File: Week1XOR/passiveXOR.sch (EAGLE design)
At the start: 27 parts

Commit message: First routing Started
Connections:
- removed net COUT: R7.2
- new net OUTC: JP1.4, R7.2
- net A: no longer JP1.2
- net B: no longer JP1.3
- net C: no longer JP1.4
- net INA: now also JP1.2
- net INB: now also JP1.3

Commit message: More routing and schmatic fixes
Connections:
- removed net VCC: JP1.1, JP2.1
- net A: no longer JP2.2
- net B: no longer JP2.3
- net C: no longer JP2.4
- net INA: now also JP2.2
- net INB: now also JP2.3
- net OUTC: now also JP2.4
- net VDD: now also JP1.1, JP2.1

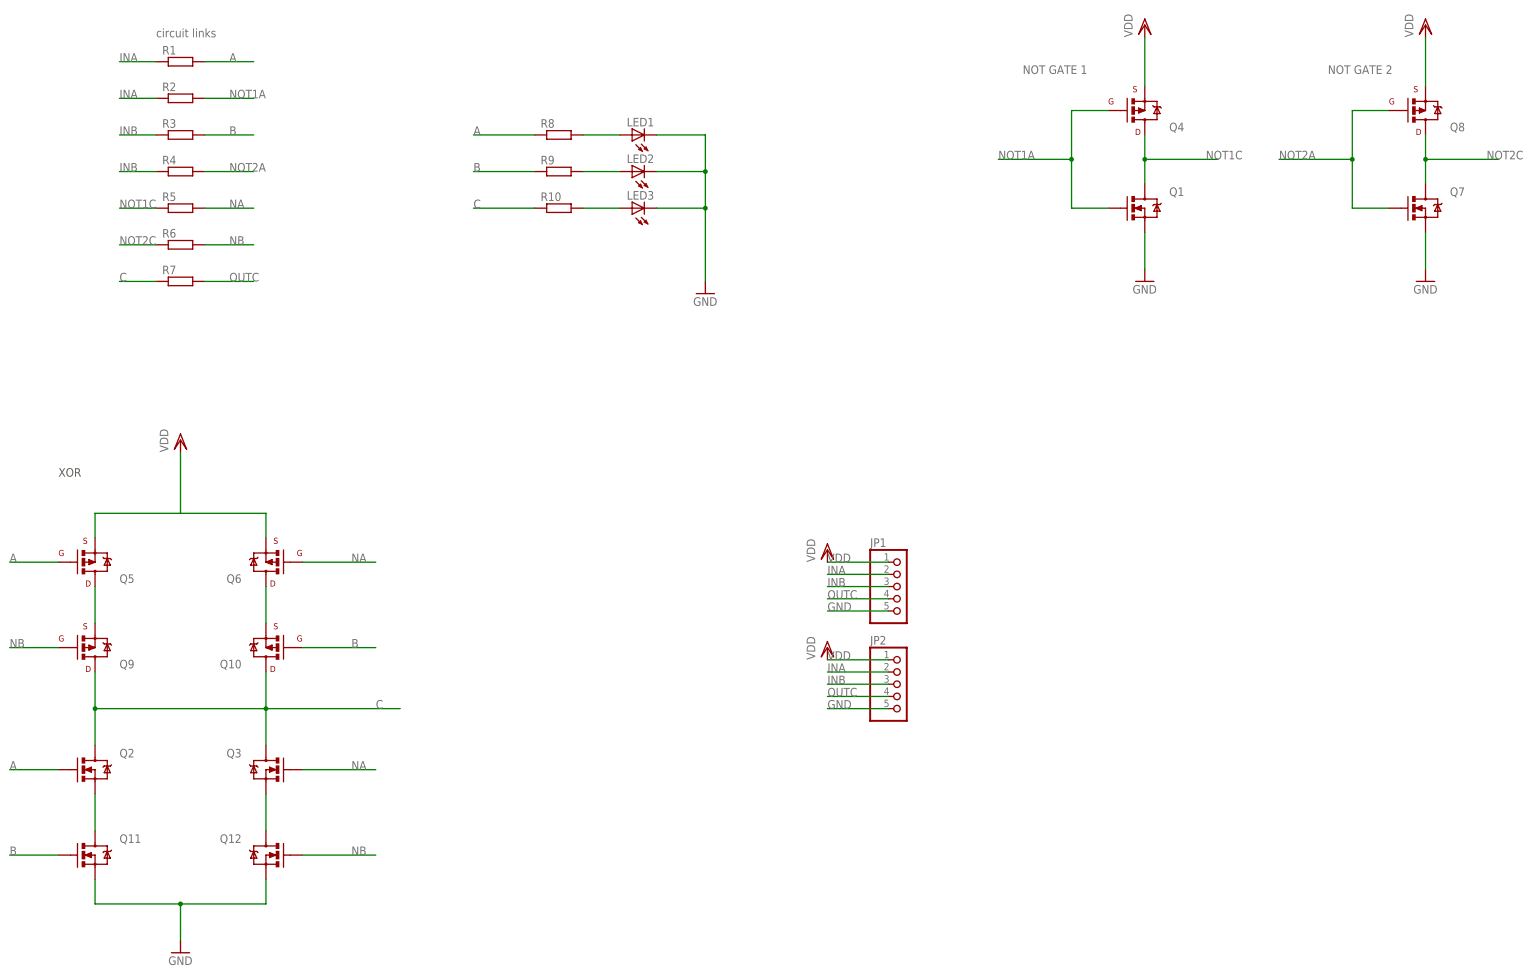
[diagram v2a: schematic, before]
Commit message: Completed ERC and more desgin tweeks
Completed ERC making sure i have vaules for parts. Changed header through holds to help with distace to the board edge.
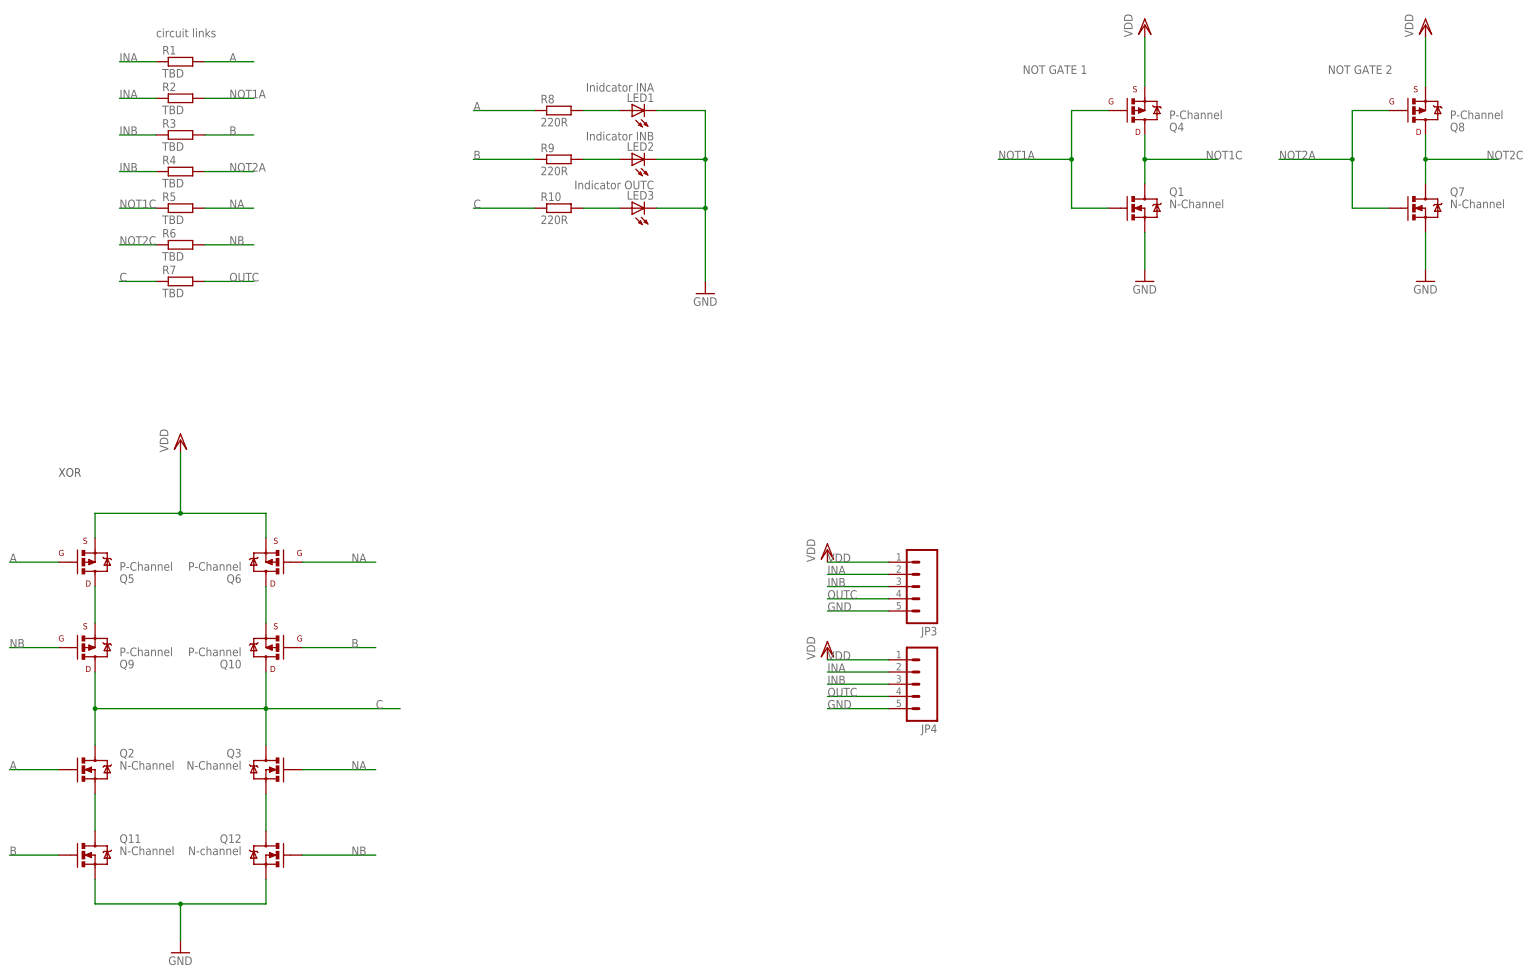
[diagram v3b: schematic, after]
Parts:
- removed JP1, JP2: (no value), pinhead:PINHD-1X5
- added JP3, JP4: (no value), SparkFun-Connectors:M05NO_SILK
- LED1: value (none) -> Inidcator INA
- LED2: value (none) -> Indicator INB
- LED3: value (none) -> Indicator OUTC
- Q1, Q11, Q2, Q3, Q7: value (none) -> N-Channel
- Q10, Q4, Q5, Q6, Q8, Q9: value (none) -> P-Channel
- Q12: value (none) -> N-channel
- R1, R2, R3, R4, R5, R6, R7: value (none) -> TBD
- R10, R8, R9: value (none) -> 220R
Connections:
- net GND: now also JP3.5, JP4.5; no longer JP1.5, JP2.5
- net INA: now also JP3.2, JP4.2; no longer JP1.2, JP2.2
- net INB: now also JP3.3, JP4.3; no longer JP1.3, JP2.3
- net OUTC: now also JP3.4, JP4.4; no longer JP1.4, JP2.4
- net VDD: now also JP3.1, JP4.1; no longer JP1.1, JP2.1
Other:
- moved on the sheet: LED1, LED2, R8, R9
